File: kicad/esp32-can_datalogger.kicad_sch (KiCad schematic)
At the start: 46 parts, among them IC2 TXU0304QPWRQ1, J1 USB_C_Receptacle_USB2.0_16P, J2 USB_C_Receptacle_USB2.0_16P, J3 USB_C_Receptacle_USB2.0_16P, J4 USB_C_Receptacle_USB2.0_16P, J5 Conn_01x04_Socket, J6 Conn_Coaxial, J7 MicroSD, SW1 SW_Push, SW2 SW_Push, SW3 SW_Push, SW4 SW_Push, U2 PA1616D, U5 TJA1051T, U6 TJA1051T, U7 ICM-20948

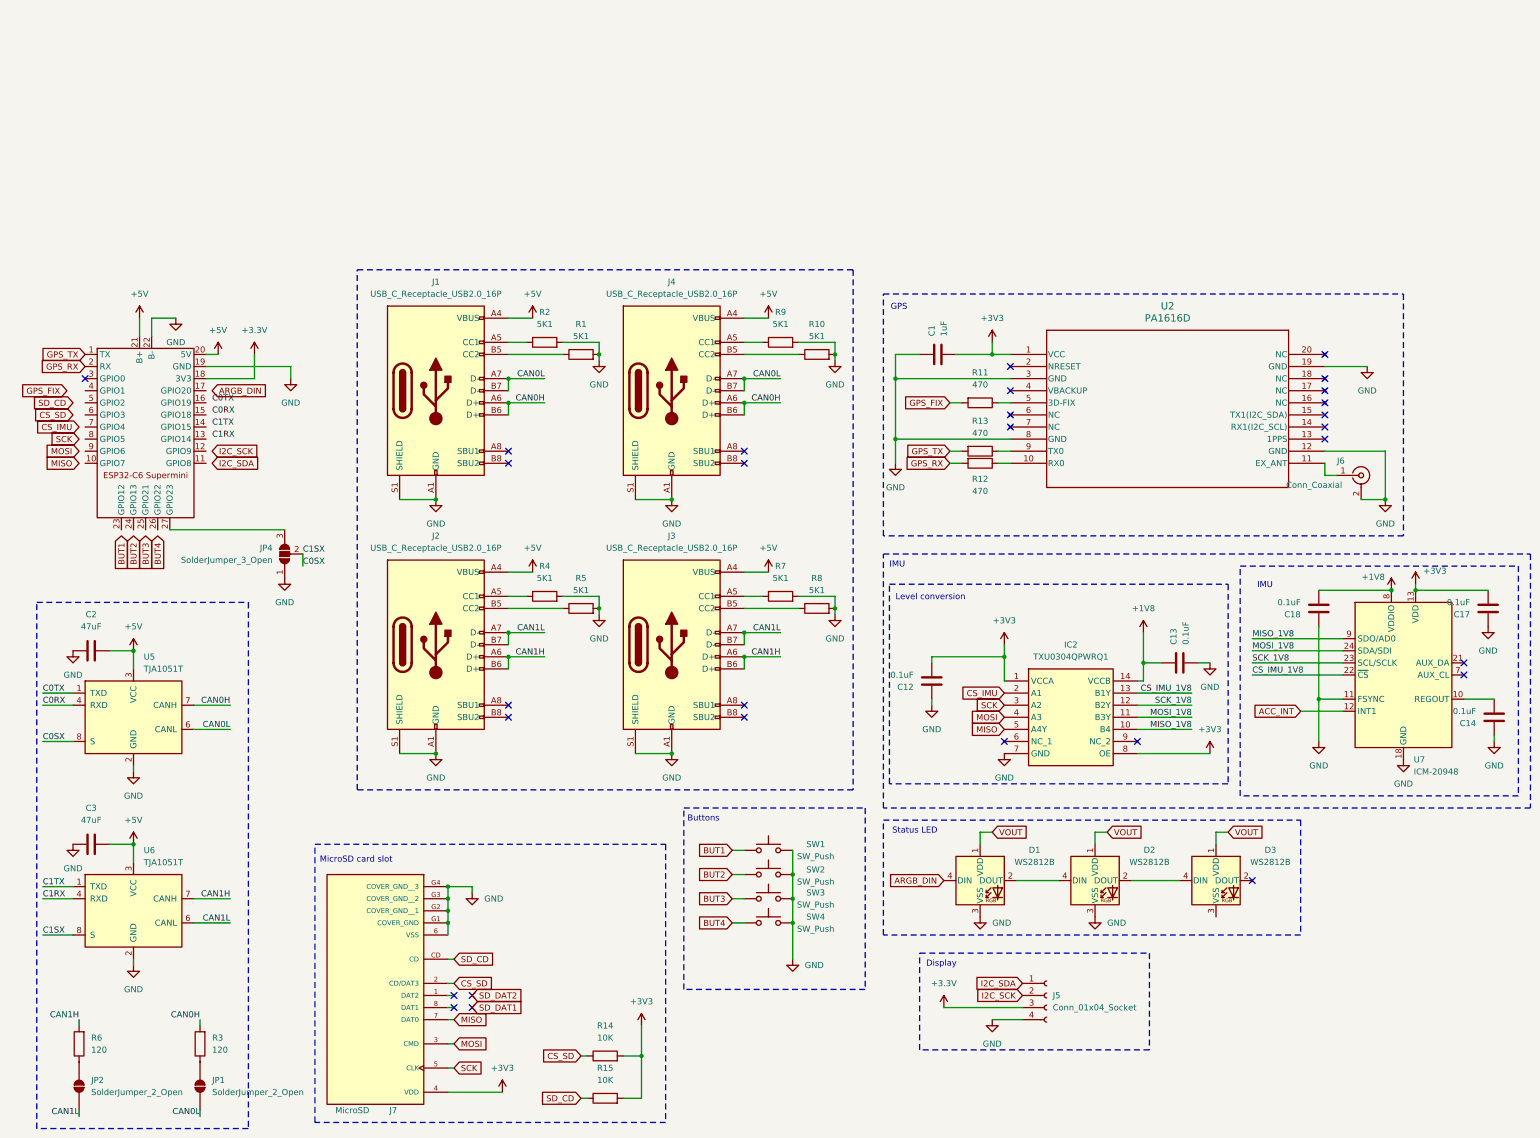
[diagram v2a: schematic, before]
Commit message: add footprints, change to bidir TTL, make connections on c6
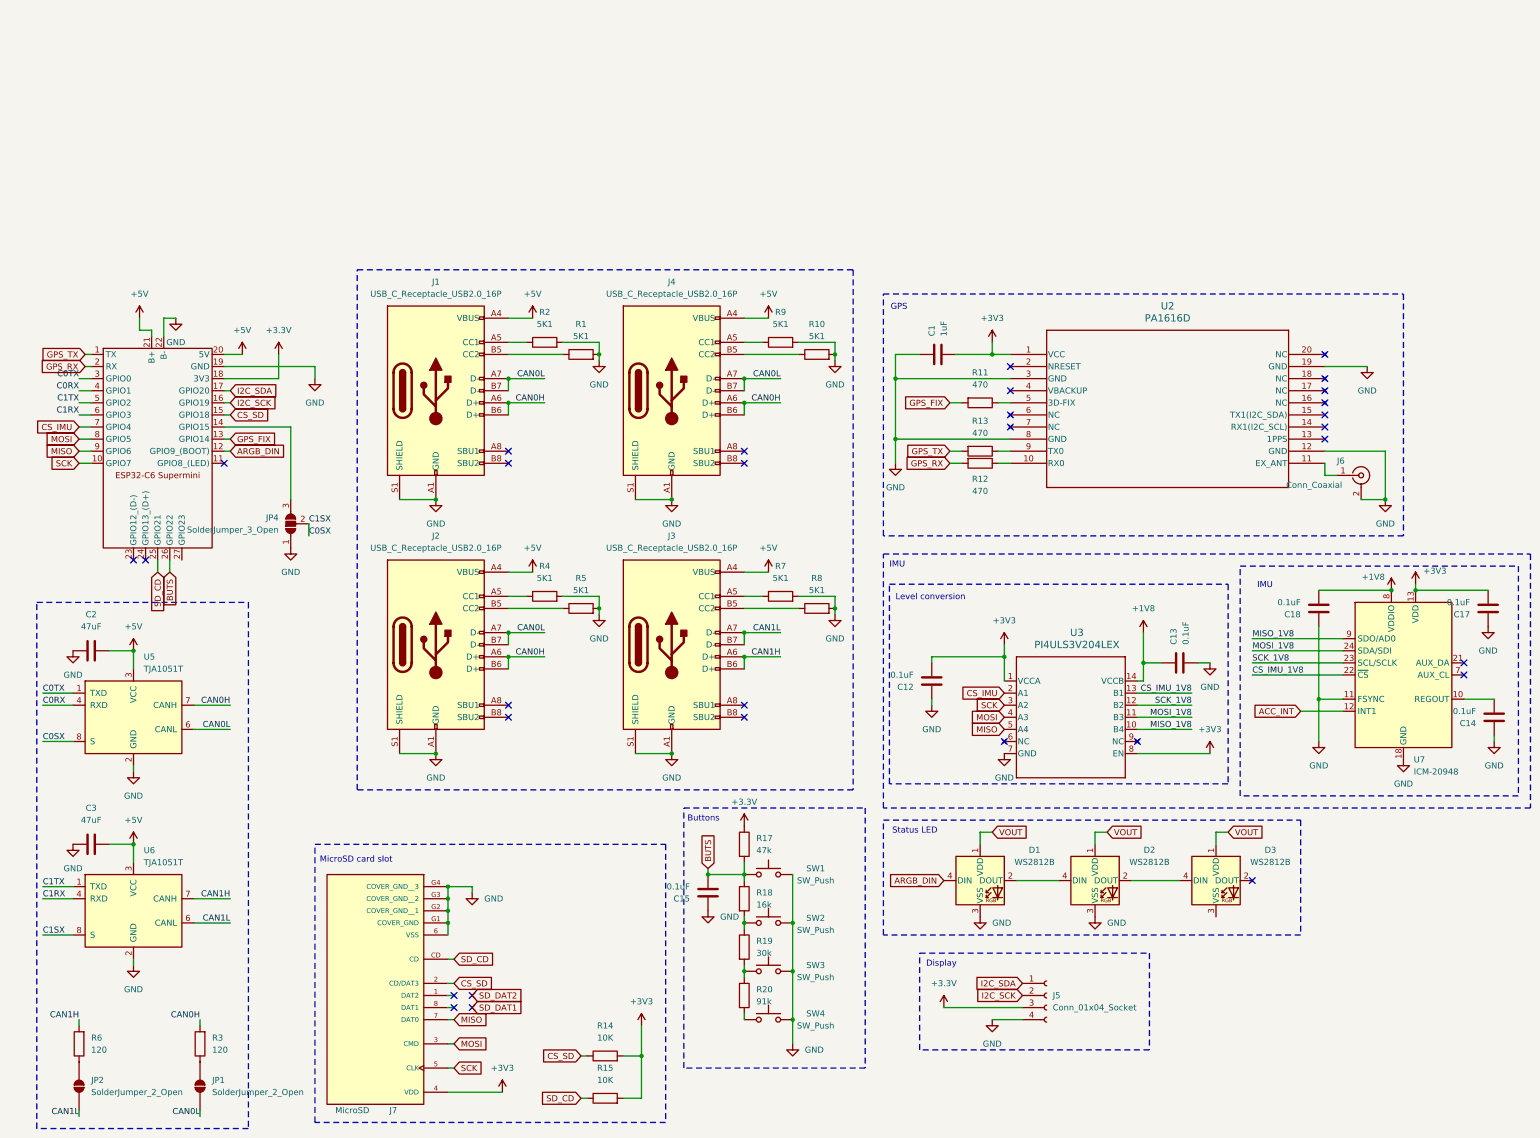
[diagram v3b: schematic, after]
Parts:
- removed IC2: TXU0304QPWRQ1, esp32-gps-lib:SOP65P640X120-14N, symbol esp32-gps-lib:TXU0304QPWRQ1
- added C15: 0.1uF, Capacitor_SMD:C_1206_3216Metric, symbol Device:C
- added R17: 47k, Resistor_SMD:R_1206_3216Metric, symbol Device:R
- added R18: 16k, Resistor_SMD:R_1206_3216Metric, symbol Device:R
- added R19: 30k, Resistor_SMD:R_1206_3216Metric, symbol Device:R
- added R20: 91k, Resistor_SMD:R_1206_3216Metric, symbol Device:R
- added U3: PI4ULS3V204LEX, esp32-can_datalogger:SOIC_3V204LEX_DIO, symbol esp32-can_datalogger:PI4ULS3V204LEX
- J5: footprint (none) -> Connector_PinSocket_2.54mm:PinSocket_1x04_P2.54mm_Vertical
- J7: footprint esp32-gps-lib:CUI_MSD-4-A -> esp32-can_datalogger:CUI_MSD-4-A
- JP4: footprint (none) -> Jumper:SolderJumper-3_P2.0mm_Open_TrianglePad1.0x1.5mm
- U2: footprint esp32-gps-lib:CD-PA1616D_ADA -> esp32-can_datalogger:CD-PA1616D_ADA
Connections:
- net BUT1 is gone; now on net BUTS: SW1.1
- net +1V8: now also U3.14 (VCCB)
- net +3.3V: now also R17.1
- net +3V3: now also U3.1 (VCCA), U3.8 (EN)
- net ARGB_DIN: now also U1.12 (GPIO9_(BOOT))
- net C0RX: now also U1.4 (GPIO1)
- net C0TX: now also U1.3 (GPIO0)
- net C1RX: now also U1.6 (GPIO3)
- net C1TX: now also U1.5 (GPIO2)
- net CAN0H: now also J2.A6 (D+), J2.B6 (D+)
- net CAN0L: now also J2.A7 (D-), J2.B7 (D-)
- net CAN1H: no longer J2.A6 (D+), J2.B6 (D+)
- net CAN1L: no longer J2.A7 (D-), J2.B7 (D-)
- net CS_IMU: now also U1.7 (GPIO4), U3.2 (A1)
- net CS_IMU_1V8: now also U3.13 (B1)
- net CS_SD: now also U1.15 (GPIO18)
- net GND: now also C15.1, U3.7 (GND)
- net GPS_FIX: now also U1.13 (GPIO14)
- net I2C_SCK: now also U1.16 (GPIO19)
- net I2C_SDA: now also U1.17 (GPIO20)
- net MISO: now also U1.9 (GPIO6), U3.5 (A4)
- net MISO_1V8: now also U3.10 (B4)
- net MOSI: now also U1.8 (GPIO5), U3.4 (A3)
- net MOSI_1V8: now also U3.11 (B3)
- net SCK: now also U1.10 (GPIO7), U3.3 (A2)
- net SCK_1V8: now also U3.12 (B2)
- net SD_CD: now also U1.25 (GPIO21)
- net at U1.14 (GPIO15): now also JP4.3 (B)
- net BUTS: now reaches U1.26 (GPIO22)
- net BUTS: now also C15.2, R17.2, R18.1
- net at U1.27 (GPIO23): no longer JP4.3 (B)
- net BUT2: no longer names the net of SW2.1
- net BUT2: now also R18.2, R19.1
- net BUT3: no longer names the net of SW3.1
- net BUT3: now also R19.2, R20.1
- net BUT4: no longer names the net of SW4.1
- net BUT4: now also R20.2
- no-connect marks 29 -> 31
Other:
- moved on the sheet: JP4, SW1, SW2, SW3, SW4

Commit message: pcb updates
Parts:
- added J8, J9: USB_C_Receptacle_USB2.0_16P, Connector_USB:USB_C_Receptacle_GCT_USB4110, symbol Connector:USB_C_Receptacle_USB2.0_16P
- added R16, R21, R22, R23: 5K1, Resistor_SMD:R_1206_3216Metric_Pad1.30x1.75mm_HandSolder, symbol Device:R
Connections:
- net +5V: now also J8.A4 (VBUS), J8.A9 (VBUS), J8.B4 (VBUS), J8.B9 (VBUS), J9.A4 (VBUS), J9.A9 (VBUS), J9.B4 (VBUS), J9.B9 (VBUS)
- net CAN0H: now also J3.A6 (D+), J3.B6 (D+), J8.A6 (D+), J8.B6 (D+), J9.A6 (D+), J9.B6 (D+); no longer J4.A6 (D+), J4.B6 (D+)
- net CAN0L: now also J3.A7 (D-), J3.B7 (D-), J8.A7 (D-), J8.B7 (D-), J9.A7 (D-), J9.B7 (D-); no longer J4.A7 (D-), J4.B7 (D-)
- net CAN1H: now also J4.A6 (D+), J4.B6 (D+); no longer J3.A6 (D+), J3.B6 (D+)
- net CAN1L: now also J4.A7 (D-), J4.B7 (D-); no longer J3.A7 (D-), J3.B7 (D-)
- net GND: now also J8.A1 (GND), J8.A12 (GND), J8.B1 (GND), J8.B12 (GND), J8.S1 (SHIELD), J9.A1 (GND), J9.A12 (GND), J9.B1 (GND), J9.B12 (GND), J9.S1 (SHIELD), R16.2, R21.2, R22.2, R23.2
- new net: J8.A5 (CC1), R16.1
- new net: J9.B5 (CC2), R23.1
- new net: J8.B5 (CC2), R21.1
- new net: J9.A5 (CC1), R22.1
- no-connect marks 31 -> 35

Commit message: pcb update
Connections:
- net +3.3V: now also C1.2, U2.1 (VCC)
- net +3V3: no longer C1.2, U2.1 (VCC)
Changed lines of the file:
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@@
 			)
 		)
-		(property "Value" "+3V3"
+		(property "Value" "+3.3V"
 			(at 214.63 22.86 0)
 			(show_name no)

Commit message: more
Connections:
- net +3V3 is gone; now on net +3.3V: C12.2, C17.2, J7.4 (VDD), R14.2, R15.2, U3.1 (VCCA), U3.8 (EN), U7.13 (VDD)
- net VOUT is gone; now on net +3.3V: D1.1 (VDD), D2.1 (VDD), D3.1 (VDD)
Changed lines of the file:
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@@
 	)
 	(junction
+		(at 261.62 133.35)
+		(diameter 0)
+		(color 0 0 0 0)
+	)
+	(junction
 		(at 147.32 5.08)
 		(diameter 0)
@@
 	)
 	(junction
+		(at 236.22 133.35)
+		(diameter 0)
+		(color 0 0 0 0)
+	)
+	(junction
 		(at 162.56 -20.32)
 		(diameter 0)
@@
 	(wire
 		(pts
-			(xy 261.62 130.81) (xy 264.16 130.81)
+			(xy 261.62 133.35) (xy 264.16 133.35)
 		)
 		(stroke
@@
 	(wire
 		(pts
-			(xy 212.09 130.81) (xy 212.09 133.35)
-		)
-		(stroke
-			(width 0)
-			(type default)
-		)
-	)
-	(wire
-		(pts
 			(xy 100.33 144.78) (xy 100.33 147.32)
 		)
@@
 	(wire
 		(pts
-			(xy 236.22 130.81) (xy 238.76 130.81)
-		)
-		(stroke
-			(width 0)
-			(type default)
-		)
-	)
-	(wire
-		(pts
 			(xy 101.6 167.64) (xy 100.33 167.64)
 		)
@@
 	(wire
 		(pts
-			(xy 261.62 130.81) (xy 261.62 133.35)
-		)
-		(stroke
-			(width 0)
-			(type default)
-		)
-	)
-	(wire
-		(pts
 			(xy 162.56 158.75) (xy 162.56 160.02)
 		)
@@
 	(wire
 		(pts
-			(xy 212.09 130.81) (xy 214.63 130.81)
+			(xy 212.09 133.35) (xy 236.22 133.35)
 		)
 		(stroke
@@
 	(wire
 		(pts
-			(xy 236.22 130.81) (xy 236.22 133.35)
-		)
-		(stroke
-			(width 0)
-			(type default)
-		)
-	)
-	(wire
-		(pts
 			(xy 101.6 175.26) (xy 100.33 175.26)
 		)
@@
 	(wire
 		(pts
+			(xy 236.22 133.35) (xy 261.62 133.35)
+		)
+		(stroke
+			(width 0)
+			(type default)
+		)
+	)
+	(wire
+		(pts
 			(xy 154.94 139.7) (xy 162.56 139.7)
 		)
@@
 		)
 	)
-	(global_label "VOUT"
-		(shape input)
-		(at 214.63 130.81 0)
-		(fields_autoplaced yes)
-		(effects
-			(font
-				(size 1.27 1.27)
-			)
-			(justify left)
-		)
-		(property "Intersheetrefs" "${INTERSHEET_REFS}"
-			(at 222.3324 130.81 0)
-			(hide yes)
-			(show_name no)
-			(do_not_autoplace no)
-			(effects
-				(font
-					(size 1.27 1.27)
-				)
-				(justify left)
-			)
-		)
-	)
 	(global_label "GPS_FIX"
 		(shape input)
@@
 		)
 	)
-	(global_label "VOUT"
-		(shape input)
-		(at 264.16 130.81 0)
-		(fields_autoplaced yes)
-		(effects
-			(font
-				(size 1.27 1.27)
-			)
-			(justify left)
-		)
-		(property "Intersheetrefs" "${INTERSHEET_REFS}"
-			(at 271.8624 130.81 0)
-			(hide yes)
-			(show_name no)
-			(do_not_autoplace no)
-			(effects
-				(font
-					(size 1.27 1.27)
-				)
-				(justify left)
-			)
-		)
-	)
 	(global_label "I2C_SDA"
 		(shape input)
@@
 		)
 	)
-	(global_label "VOUT"
-		(shape input)
-		(at 238.76 130.81 0)
-		(fields_autoplaced yes)
-		(effects
-			(font
-				(size 1.27 1.27)
-			)
-			(justify left)
-		)
-		(property "Intersheetrefs" "${INTERSHEET_REFS}"
-			(at 246.4624 130.81 0)
-			(hide yes)
-			(show_name no)
-			(do_not_autoplace no)
-			(effects
-				(font
-					(size 1.27 1.27)
-				)
-				(justify left)
-			)
-		)
-	)
 	(global_label "ARGB_DIN"
 		(shape input)
@@
 			)
 		)
-		(property "Value" "+3V3"
+		(property "Value" "+3.3V"
 			(at 260.35 109.22 0)
 			(show_name no)
@@
 			)
 		)
-		(property "Value" "+3V3"
+		(property "Value" "+3.3V"
 			(at 217.17 86.36 0)
 			(show_name no)
@@
 	(symbol
 		(lib_id "power:+3.3V")
+		(at 264.16 133.35 0)
+		(unit 1)
+		(body_style 1)
+		(exclude_from_sim no)
+		(in_bom yes)
+		(on_board yes)
+		(in_pos_files yes)
+		(dnp no)
+		(fields_autoplaced yes)
+		(property "Reference" "#PWR057"
+			(at 264.16 137.16 0)
+			(hide yes)
+			(show_name no)
+			(do_not_autoplace no)
+			(effects
+				(font
+					(size 1.27 1.27)
+				)
+			)
+		)
+		(property "Value" "+3.3V"
+			(at 264.16 128.27 0)
+			(show_name no)
+			(do_not_autoplace no)
+			(effects
+				(font
+					(size 1.27 1.27)
+				)
+			)
+		)
+		(property "Footprint" ""
+			(at 264.16 133.35 0)
+			(hide yes)
+			(show_name no)
+			(do_not_autoplace no)
+			(effects
+				(font
+					(size 1.27 1.27)
+				)
+			)
+		)
+		(property "Datasheet" ""
+			(at 264.16 133.35 0)
+			(hide yes)
+			(show_name no)
+			(do_not_autoplace no)
+			(effects
+				(font
+					(size 1.27 1.27)
+				)
+			)
+		)
+		(property "Description" "Power symbol creates a global label with name \"+3.3V\""
+			(at 264.16 133.35 0)
+			(hide yes)
+			(show_name no)
+			(do_not_autoplace no)
+			(effects
+				(font
+					(size 1.27 1.27)
+				)
+			)
+		)
+		(pin "1"
+		)
+		(instances
+			(project "esp32-can_datalogger"
+				(path "/27d88dad-6a90-4f6f-a0dd-ec7ff61f0111"
+					(reference "#PWR057")
+					(unit 1)
+				)
+			)
+		)
+	)
+	(symbol
+		(lib_id "power:+3.3V")
 		(at 298.45 80.01 0)
 		(unit 1)
@@
 			)
 		)
-		(property "Value" "+3V3"
+		(property "Value" "+3.3V"
 			(at 111.76 180.34 0)
 			(show_name no)
@@
 			)
 		)
-		(property "Value" "+3V3"
+		(property "Value" "+3.3V"
 			(at 307.594 75.946 0)
 			(show_name no)
@@
 			)
 		)
-		(property "Value" "+3V3"
+		(property "Value" "+3.3V"
 			(at 140.97 166.37 0)
 			(show_name no)

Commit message: add vreg
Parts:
- added C4: 10uF, Capacitor_SMD:C_1206_3216Metric, symbol Device:C
- added C5: 22uF, Capacitor_SMD:C_1206_3216Metric, symbol Device:C
- added U4: AZ1117-1.8, Package_TO_SOT_SMD:SOT-223-3_TabPin2, symbol Regulator_Linear:AZ1117-1.8
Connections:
- net +1V8: now also C5.1, U4.2 (VO)
- net +5V: now also C4.1, U4.3 (VI)
- net GND: now also C4.2, C5.2, U4.1 (GND)

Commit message: minor updates
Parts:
- renumbered J8 to J4, J9 to J5, J4 to J6, J6 to J7, J7 to J8, J5 to J9, JP4 to JP3
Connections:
- net GND: now also D3.3 (VSS)
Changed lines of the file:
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@@
 		(dnp no)
 		(fields_autoplaced yes)
-		(property "Reference" "J4"
+		(property "Reference" "J6"
 			(at 147.32 15.24 0)
 			(show_name no)
@@
 			(project "esp32-can_datalogger"
 				(path "/27d88dad-6a90-4f6f-a0dd-ec7ff61f0111"
-					(reference "J4")
+					(reference "J6")
 					(unit 1)
 				)
@@
 		(in_pos_files yes)
 		(dnp no)
-		(property "Reference" "J6"
+		(property "Reference" "J7"
 			(at 287.02 52.832 0)
 			(show_name no)
@@
 			(project "esp32-can_datalogger"
 				(path "/27d88dad-6a90-4f6f-a0dd-ec7ff61f0111"
-					(reference "J6")
+					(reference "J7")
 					(unit 1)
 				)
@@
 		(dnp no)
 		(fields_autoplaced yes)
-		(property "Reference" "J8"
-			(at 97.79 -40.64 0)
+		(property "Reference" "J4"
+			(at 97.79 -39.37 0)
 			(show_name no)
 			(do_not_autoplace no)
@@
 		)
 		(property "Value" "USB_C_Receptacle_USB2.0_16P"
-			(at 97.79 -38.1 0)
+			(at 97.79 -36.83 0)
 			(show_name no)
 			(do_not_autoplace no)
@@
 			(project "esp32-can_datalogger"
 				(path "/27d88dad-6a90-4f6f-a0dd-ec7ff61f0111"
-					(reference "J8")
+					(reference "J4")
 					(unit 1)
 				)
@@
 		(in_pos_files yes)
 		(dnp no)
-		(property "Reference" "J7"
+		(property "Reference" "J8"
 			(at 89.662 189.23 0)
 			(show_name no)
@@
 			(project "esp32-can_datalogger"
 				(path "/27d88dad-6a90-4f6f-a0dd-ec7ff61f0111"
-					(reference "J7")
+					(reference "J8")
 					(unit 1)
 				)
@@
 	(symbol
 		(lib_id "power:GND")
+		(at 261.62 148.59 0)
+		(unit 1)
+		(body_style 1)
+		(exclude_from_sim no)
+		(in_bom yes)
+		(on_board yes)
+		(in_pos_files yes)
+		(dnp no)
+		(fields_autoplaced yes)
+		(property "Reference" "#PWR061"
+			(at 261.62 154.94 0)
+			(hide yes)
+			(show_name no)
+			(do_not_autoplace no)
+			(effects
+				(font
+					(size 1.27 1.27)
+				)
+			)
+		)
+		(property "Value" "GND"
+			(at 264.16 149.8599 0)
+			(show_name no)
+			(do_not_autoplace no)
+			(effects
+				(font
+					(size 1.27 1.27)
+				)
+				(justify left)
+			)
+		)
+		(property "Footprint" ""
+			(at 261.62 148.59 0)
+			(hide yes)
+			(show_name no)
+			(do_not_autoplace no)
+			(effects
+				(font
+					(size 1.27 1.27)
+				)
+			)
+		)
+		(property "Datasheet" ""
+			(at 261.62 148.59 0)
+			(hide yes)
+			(show_name no)
+			(do_not_autoplace no)
+			(effects
+				(font
+					(size 1.27 1.27)
+				)
+			)
+		)
+		(property "Description" "Power symbol creates a global label with name \"GND\" , ground"
+			(at 261.62 148.59 0)
+			(hide yes)
+			(show_name no)
+			(do_not_autoplace no)
+			(effects
+				(font
+					(size 1.27 1.27)
+				)
+			)
+		)
+		(pin "1"
+		)
+		(instances
+			(project "esp32-can_datalogger"
+				(path "/27d88dad-6a90-4f6f-a0dd-ec7ff61f0111"
+					(reference "#PWR061")
+					(unit 1)
+				)
+			)
+		)
+	)
+	(symbol
+		(lib_id "power:GND")
 		(at 97.79 5.08 0)
 		(unit 1)
@@
 		(dnp no)
 		(fields_autoplaced yes)
-		(property "Reference" "J9"
-			(at 147.32 -40.64 0)
+		(property "Reference" "J5"
+			(at 147.32 -39.37 0)
 			(show_name no)
 			(do_not_autoplace no)
@@
 		)
 		(property "Value" "USB_C_Receptacle_USB2.0_16P"
-			(at 147.32 -38.1 0)
+			(at 147.32 -36.83 0)
 			(show_name no)
 			(do_not_autoplace no)
@@
 			(project "esp32-can_datalogger"
 				(path "/27d88dad-6a90-4f6f-a0dd-ec7ff61f0111"
-					(reference "J9")
+					(reference "J5")
 					(unit 1)
 				)
@@
 		(dnp no)
 		(fields_autoplaced yes)
-		(property "Reference" "JP4"
+		(property "Reference" "JP3"
 			(at 64.77 64.7699 90)
 			(show_name no)
@@
 			(project "esp32-can_datalogger"
 				(path "/27d88dad-6a90-4f6f-a0dd-ec7ff61f0111"
-					(reference "JP4")
+					(reference "JP3")
 					(unit 1)
 				)
@@
 		(dnp no)
 		(fields_autoplaced yes)
-		(property "Reference" "J5"
+		(property "Reference" "J9"
 			(at 227.33 165.0999 0)
 			(show_name no)
@@
 			(project "esp32-can_datalogger"
 				(path "/27d88dad-6a90-4f6f-a0dd-ec7ff61f0111"
-					(reference "J5")
+					(reference "J9")
 					(unit 1)
 				)
